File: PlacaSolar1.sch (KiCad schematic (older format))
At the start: 30 parts, among them J1 Jack-DC, J2 Conn_01x05_Female, J4 Conn_01x15_Female, J5 Conn_01x15_Female, J6 Conn_01x04_Female, SW1 SW_SPDT, U1 L7805

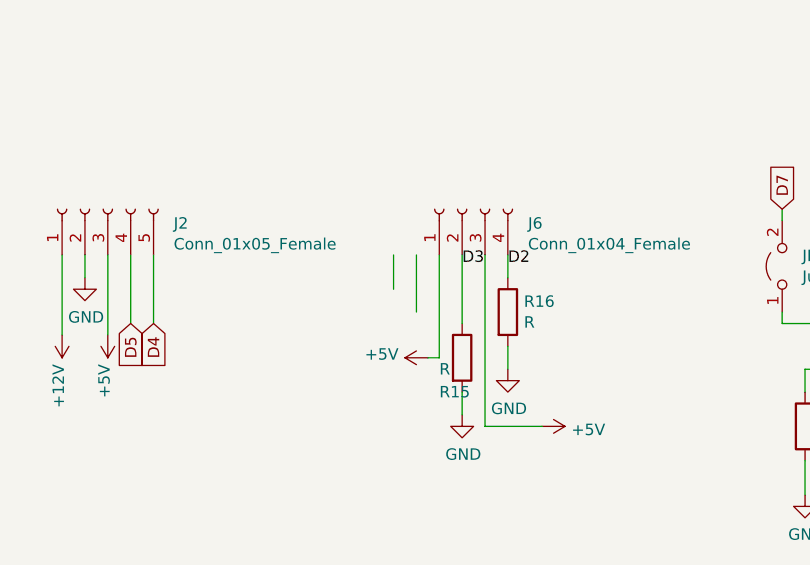
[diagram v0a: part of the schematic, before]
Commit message: Corrigindo tamanho dos bornes 7x7cm
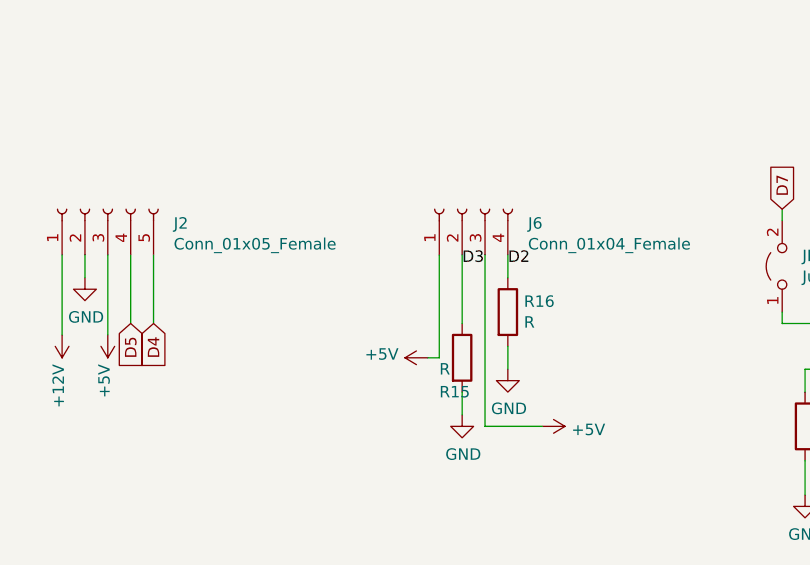
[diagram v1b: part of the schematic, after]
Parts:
- J6: footprint TerminalBlock:TerminalBlock_bornier-4_P5.08mm -> Painel-Solar:Borne_LAB_4
- R1, R2, R5, R6, R7, R8: footprint TerminalBlock:TerminalBlock_bornier-2_P5.08mm -> Painel-Solar:Borne_LAB_2
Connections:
- wire segments 108 -> 106
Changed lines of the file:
@@
 F 0 "R7" V 2150 5300 50  0000 C CNN
 F 1 "LDR03" V 1950 5600 50  0000 C CNN
-F 2 "TerminalBlock:TerminalBlock_bornier-2_P5.08mm" V 2225 5400 50  0001 C CNN
+F 2 "Painel-Solar:Borne_LAB_2" V 2225 5400 50  0001 C CNN
 F 3 "http://www.elektronica-componenten.nl/WebRoot/StoreNL/Shops/61422969/54F1/BA0C/C664/31B9/2173/C0A8/2AB9/2AEF/LDR03IMP.pdf" H 2050 5350 50  0001 C CNN
 	1    2050 5400
@@
 F 0 "R8" V 2150 5700 50  0000 C CNN
 F 1 "LDR03" V 1950 6000 50  0000 C CNN
-F 2 "TerminalBlock:TerminalBlock_bornier-2_P5.08mm" V 2225 5800 50  0001 C CNN
+F 2 "Painel-Solar:Borne_LAB_2" V 2225 5800 50  0001 C CNN
 F 3 "http://www.elektronica-componenten.nl/WebRoot/StoreNL/Shops/61422969/54F1/BA0C/C664/31B9/2173/C0A8/2AB9/2AEF/LDR03IMP.pdf" H 2050 5750 50  0001 C CNN
 	1    2050 5800
@@
 F 0 "R5" V 2150 4500 50  0000 C CNN
 F 1 "LDR03" V 1950 4800 50  0000 C CNN
-F 2 "TerminalBlock:TerminalBlock_bornier-2_P5.08mm" V 2225 4600 50  0001 C CNN
+F 2 "Painel-Solar:Borne_LAB_2" V 2225 4600 50  0001 C CNN
 F 3 "http://www.elektronica-componenten.nl/WebRoot/StoreNL/Shops/61422969/54F1/BA0C/C664/31B9/2173/C0A8/2AB9/2AEF/LDR03IMP.pdf" H 2050 4550 50  0001 C CNN
 	1    2050 4600
@@
 F 0 "R6" V 2150 4900 50  0000 C CNN
 F 1 "LDR03" V 1950 5200 50  0000 C CNN
-F 2 "TerminalBlock:TerminalBlock_bornier-2_P5.08mm" V 2225 5000 50  0001 C CNN
+F 2 "Painel-Solar:Borne_LAB_2" V 2225 5000 50  0001 C CNN
 F 3 "http://www.elektronica-componenten.nl/WebRoot/StoreNL/Shops/61422969/54F1/BA0C/C664/31B9/2173/C0A8/2AB9/2AEF/LDR03IMP.pdf" H 2050 4950 50  0001 C CNN
 	1    2050 5000
@@
 	1    0    0    -1
 $EndComp
-Wire Wire Line
-	6050 4700 6050 4950
-Wire Wire Line
-	5950 4700 5950 4850
 Text GLabel 4900 5000 3    50   Input ~ 0
 D4
@@
 F 0 "R1" V 2200 3700 50  0000 C CNN
 F 1 "LDR03" V 2000 4000 50  0000 C CNN
-F 2 "TerminalBlock:TerminalBlock_bornier-2_P5.08mm" V 2275 3800 50  0001 C CNN
+F 2 "Painel-Solar:Borne_LAB_2" V 2275 3800 50  0001 C CNN
 F 3 "http://www.elektronica-componenten.nl/WebRoot/StoreNL/Shops/61422969/54F1/BA0C/C664/31B9/2173/C0A8/2AB9/2AEF/LDR03IMP.pdf" H 2100 3750 50  0001 C CNN
 	1    2100 3800
@@
 F 0 "R2" V 2200 4100 50  0000 C CNN
 F 1 "LDR03" V 2000 4400 50  0000 C CNN
-F 2 "TerminalBlock:TerminalBlock_bornier-2_P5.08mm" V 2275 4200 50  0001 C CNN
+F 2 "Painel-Solar:Borne_LAB_2" V 2275 4200 50  0001 C CNN
 F 3 "http://www.elektronica-componenten.nl/WebRoot/StoreNL/Shops/61422969/54F1/BA0C/C664/31B9/2173/C0A8/2AB9/2AEF/LDR03IMP.pdf" H 2100 4150 50  0001 C CNN
 	1    2100 4200
@@
 	-1   0    0    1
 $EndComp
-$Comp
-L Connector:Conn_01x04_Female J6
-U 1 1 61473C9D
-P 6250 4500
-F 0 "J6" V 6188 4212 50  0000 R CNN
-F 1 "Conn_01x04_Female" V 6097 4212 50  0000 R CNN
-F 2 "TerminalBlock:TerminalBlock_bornier-4_P5.08mm" H 6250 4500 50  0001 C CNN
-F 3 "~" H 6250 4500 50  0001 C CNN
-	1    6250 4500
-	0    -1   -1   0
-$EndComp
 Wire Wire Line
 	4600 4800 4600 4700
@@
 	1    0    0    -1
 $EndComp
+$Comp
+L Connector:Conn_01x04_Female J6
+U 1 1 61473C9D
+P 6250 4500
+F 0 "J6" V 6188 4212 50  0000 R CNN
+F 1 "Conn_01x04_Female" V 6097 4212 50  0000 R CNN
+F 2 "Painel-Solar:Borne_LAB_4" H 6250 4500 50  0001 C CNN
+F 3 "~" H 6250 4500 50  0001 C CNN
+	1    6250 4500
+	0    -1   -1   0
+$EndComp
 $EndSCHEMATC
